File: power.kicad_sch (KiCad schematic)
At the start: 20 parts, among them J3 Conn_01x02, Q2 AO3401A, SW8 SW_Slide_DPDT, U3 TP4056-42-ESOP8, U7 TPS62160DGK

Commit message: whole bunch of layout done
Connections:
- net +3.3V renamed +3V3
- net +5V renamed VDC

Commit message: more routing
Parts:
- J3: footprint Connector_JST:JST_PH_B2B-PH-K_1x02_P2.00mm_Vertical -> Connector_JST:JST_PH_S2B-PH-SM4-TB_1x02-1MP_P2.00mm_Horizontal; LCSC C131337 -> C295747; Manufacturer Part Number B2B-PH-K-S(LF)(SN) -> S2B-PH-SM4-TB(LF)(SN)
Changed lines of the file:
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@@
 			)
 		)
-		(property "Footprint" "Connector_JST:JST_PH_B2B-PH-K_1x02_P2.00mm_Vertical"
+		(property "Footprint" "Connector_JST:JST_PH_S2B-PH-SM4-TB_1x02-1MP_P2.00mm_Horizontal"
 			(at 146.05 124.46 0)
 			(effects
@@
 			)
 		)
-		(property "LCSC" "C131337"
+		(property "LCSC" "C295747"
 			(at 146.05 124.46 0)
 			(effects
@@
 			)
 		)
-		(property "Manufacturer Part Number" "B2B-PH-K-S(LF)(SN)"
+		(property "Manufacturer Part Number" "S2B-PH-SM4-TB(LF)(SN)"
 			(at 146.05 124.46 0)
 			(effects

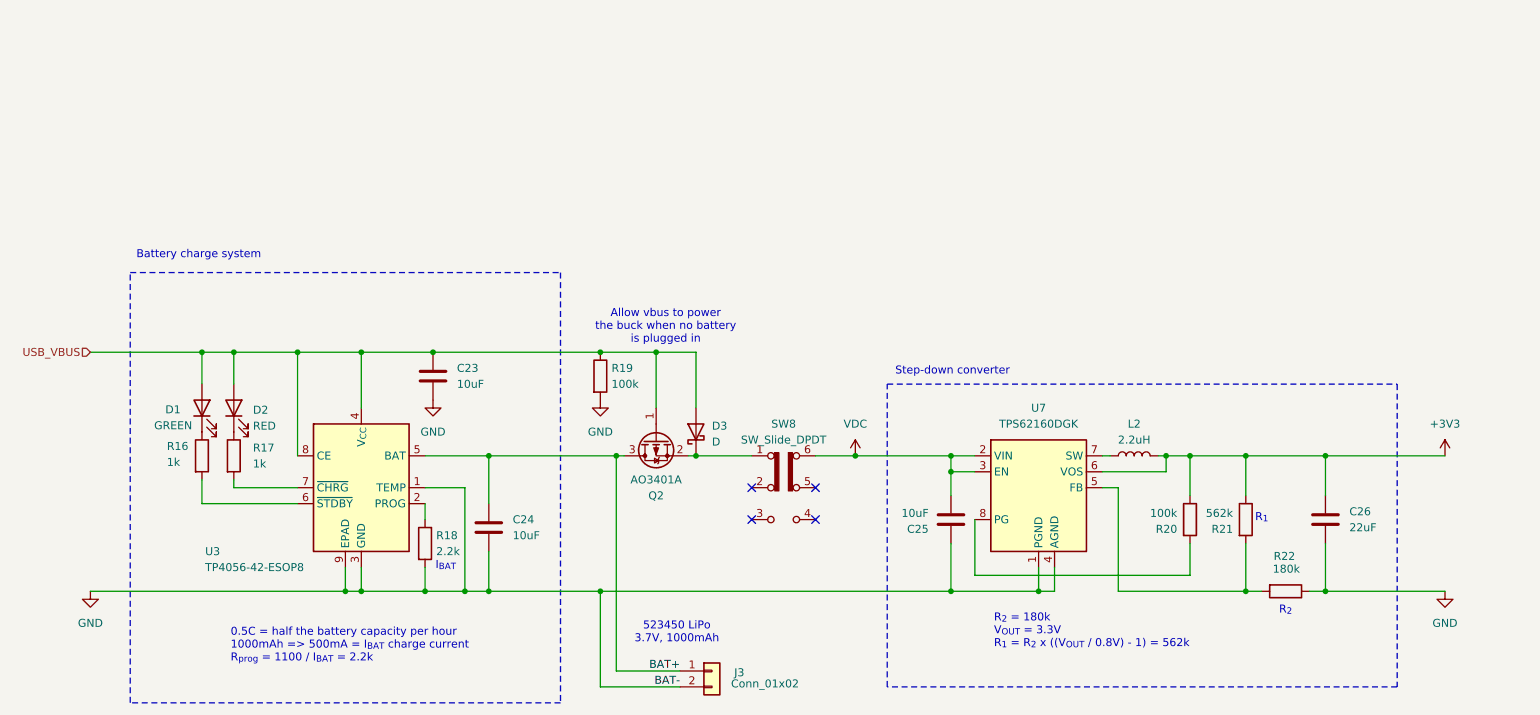
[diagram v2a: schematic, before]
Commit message: add silkscreen, optimize layout and replace sd card peripheral
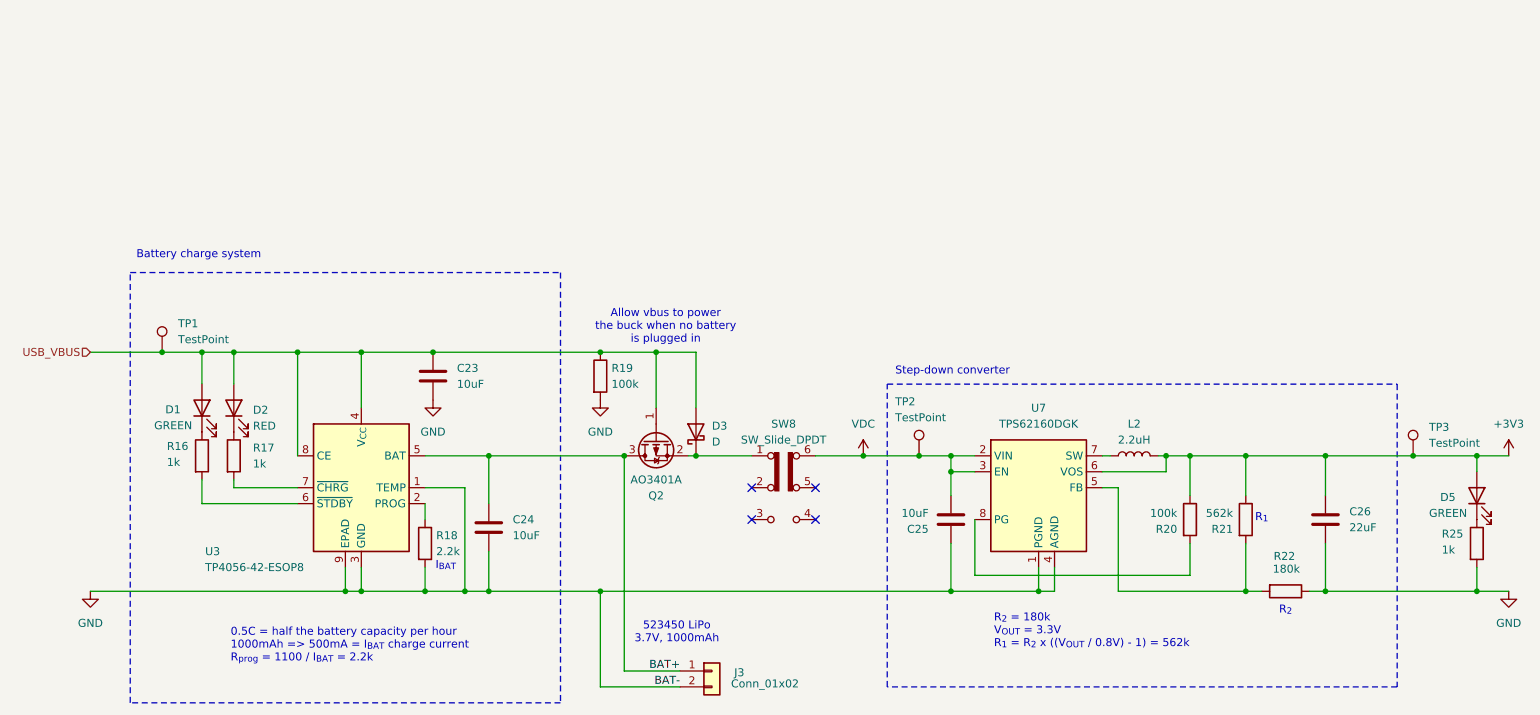
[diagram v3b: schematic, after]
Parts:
- added D5: GREEN, LED_SMD:LED_0603_1608Metric, symbol Device:LED
- added R25: 1k, Resistor_SMD:R_0603_1608Metric, symbol Device:R
- added TP1, TP2, TP3: TestPoint, TestPoint:TestPoint_Pad_D1.0mm, symbol Connector:TestPoint
- D1: LCSC C965804 -> C22371297; Manufacturer XINGLIGHT -> HONGLITRONIC; Manufacturer Part Number XL-1608UGC-04 -> PSC-1608U52GC-G4
- D2: LCSC C965799 -> C2286; Manufacturer XINGLIGHT -> Hubei KENTO Elec; Manufacturer Part Number XL-1608SURC-06 -> KT-0603R
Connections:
- net +3V3: now also D5.2 (A), TP3.1
- net GND: now also R25.2
- net USB_VBUS: now also TP1.1
- net VDC: now also TP2.1
- new net: D5.1 (K), R25.1

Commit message: add power monitoring
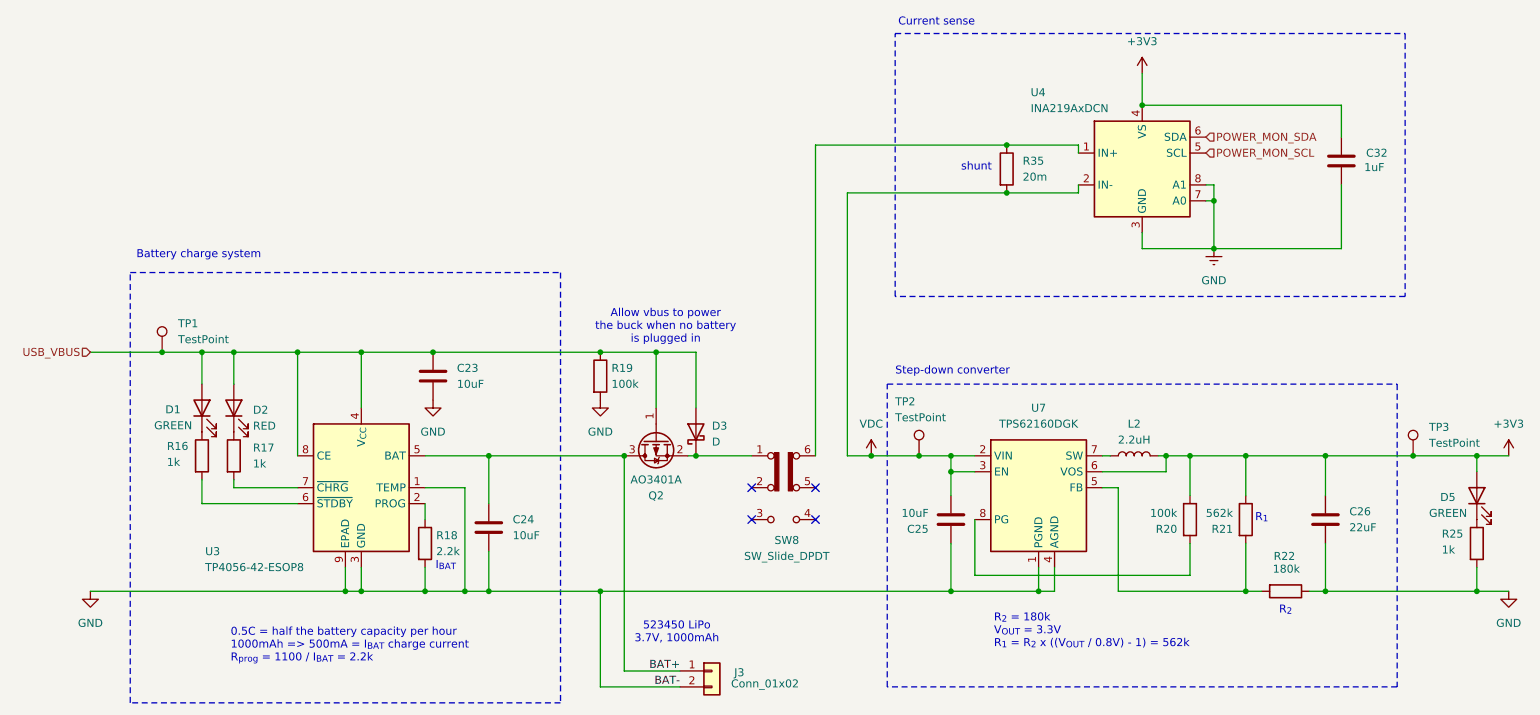
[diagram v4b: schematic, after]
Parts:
- added C32: 1uF, Capacitor_SMD:C_0402_1005Metric, symbol Device:C
- added R35: 20m, Resistor_SMD:R_1206_3216Metric, symbol Device:R
- added U4: INA219AxDCN, Package_TO_SOT_SMD:SOT-23-8, symbol Sensor_Energy:INA219AxDCN
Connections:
- net +3V3: now also C32.2, U4.4 (VS)
- net GND: now also C32.1, U4.3 (GND), U4.7 (A0), U4.8 (A1)
- net VDC: now also R35.2, U4.2 (IN-); no longer SW8.6 (C)
- new net: R35.1, SW8.6 (C), U4.1 (IN+)
- new net POWER_MON_SCL: U4.5 (SCL)
- new net POWER_MON_SDA: U4.6 (SDA)
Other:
- note added: "Current sense"
- note added: "shunt"

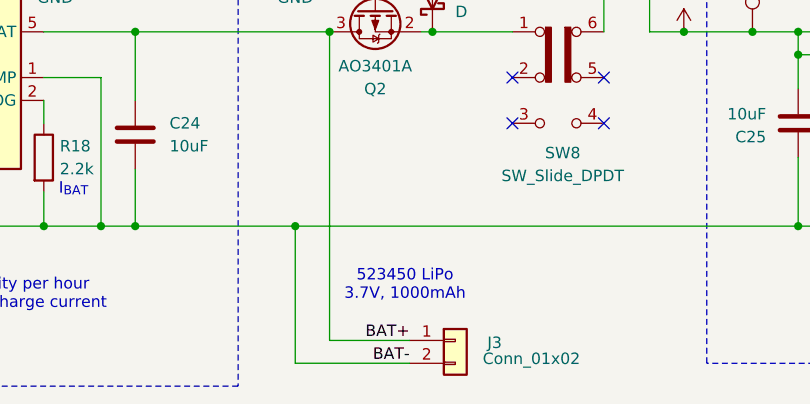
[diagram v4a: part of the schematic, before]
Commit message: proper lcd backlight driver
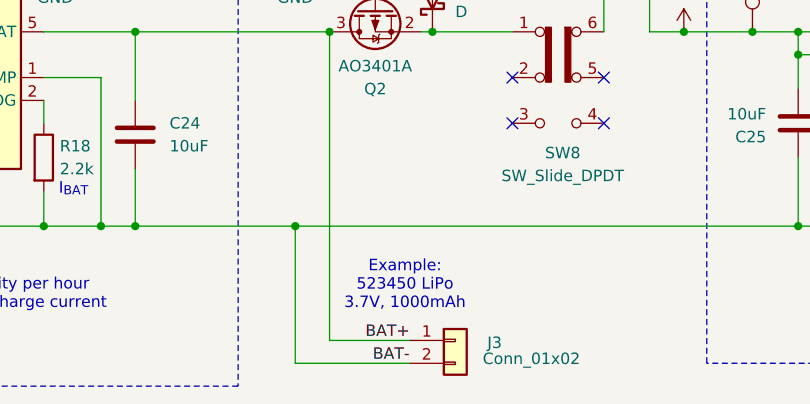
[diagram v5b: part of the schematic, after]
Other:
- note added: "Example: 523450 LiPo 3.7V, 1000mAh"
- note removed: "523450 LiPo 3.7V, 1000mAh"
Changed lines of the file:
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@@
 		)
 	)
-	(text "523450 LiPo\n3.7V, 1000mAh"
+	(text "Example:\n523450 LiPo\n3.7V, 1000mAh"
 		(exclude_from_sim no)
 		(at 140.462 118.364 0)

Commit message: changes for production
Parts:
- TP1, TP2, TP3: now left out of the parts list
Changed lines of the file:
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@@
 		(unit 1)
 		(exclude_from_sim no)
-		(in_bom yes)
+		(in_bom no)
 		(on_board yes)
 		(dnp no)
@@
 		(unit 1)
 		(exclude_from_sim no)
-		(in_bom yes)
+		(in_bom no)
 		(on_board yes)
 		(dnp no)
@@
 		(unit 1)
 		(exclude_from_sim no)
-		(in_bom yes)
-		(on_board yes)
-		(dnp no)
+		(in_bom no)
+		(on_board yes)
+		(dnp no)

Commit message: fix bom
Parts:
- C32: LCSC C52923 -> (none)
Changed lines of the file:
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@@
 			)
 		)
-		(property "LCSC" "C52923"
+		(property "LCSC" ""
 			(at 246.38 43.18 0)
 			(effects

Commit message: align some components with inventory
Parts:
- C23, C24, C25: footprint Capacitor_SMD:C_0603_1608Metric -> Capacitor_SMD:C_0805_2012Metric
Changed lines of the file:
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@@
 			)
 		)
-		(property "Footprint" "Capacitor_SMD:C_0603_1608Metric"
+		(property "Footprint" "Capacitor_SMD:C_0805_2012Metric"
 			(at 111.4552 105.41 0)
 			(effects
@@
 			)
 		)
-		(property "Footprint" "Capacitor_SMD:C_0603_1608Metric"
+		(property "Footprint" "Capacitor_SMD:C_0805_2012Metric"
 			(at 185.1152 104.14 0)
 			(effects
@@
 			)
 		)
-		(property "Footprint" "Capacitor_SMD:C_0603_1608Metric"
+		(property "Footprint" "Capacitor_SMD:C_0805_2012Metric"
 			(at 102.5652 81.28 0)
 			(effects
